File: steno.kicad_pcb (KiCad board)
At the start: 4 copper layers, 220 x 59 mm, 83 parts, among them J1 USB_C_Receptacle_USB2.0_14P, U1 W25Q16JVSS, U2 AP2127N-3.3, U3 RP2040, Y1 12 MHz

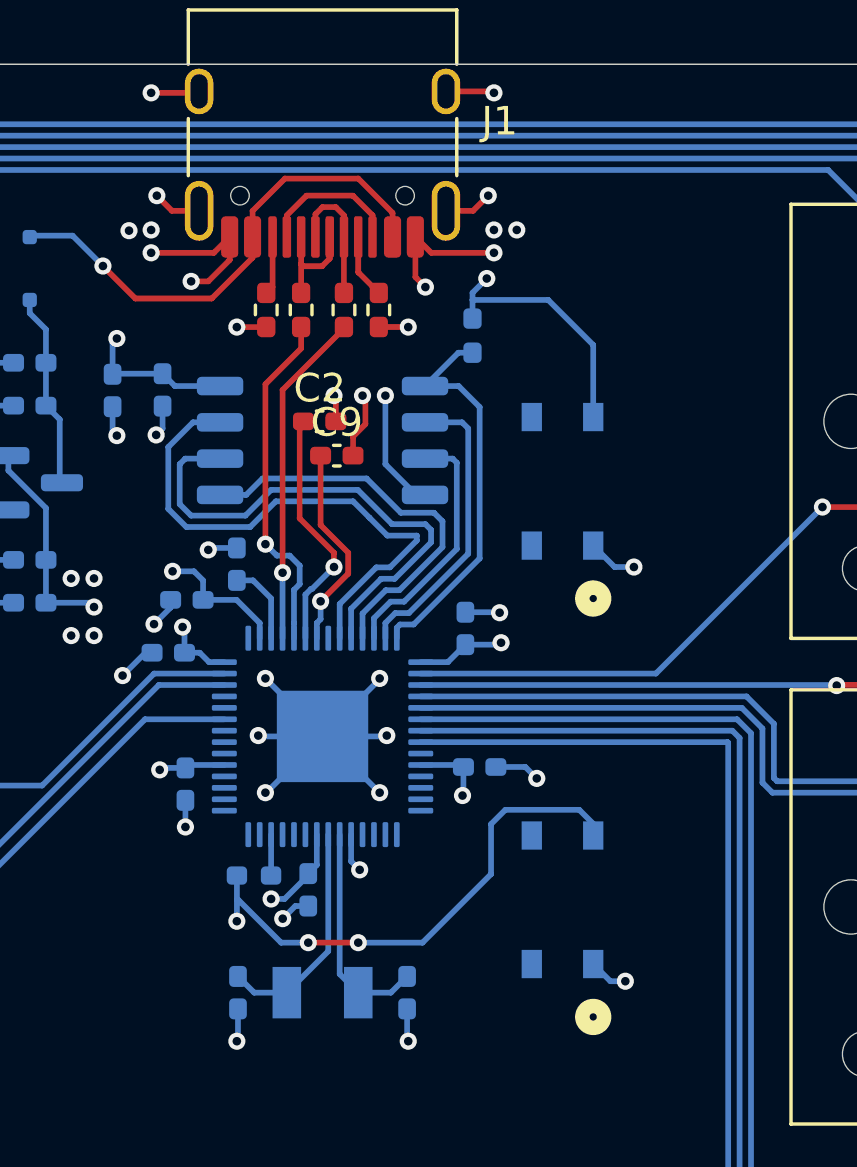
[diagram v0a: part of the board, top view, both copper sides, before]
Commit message: added status LED / Potential final changes
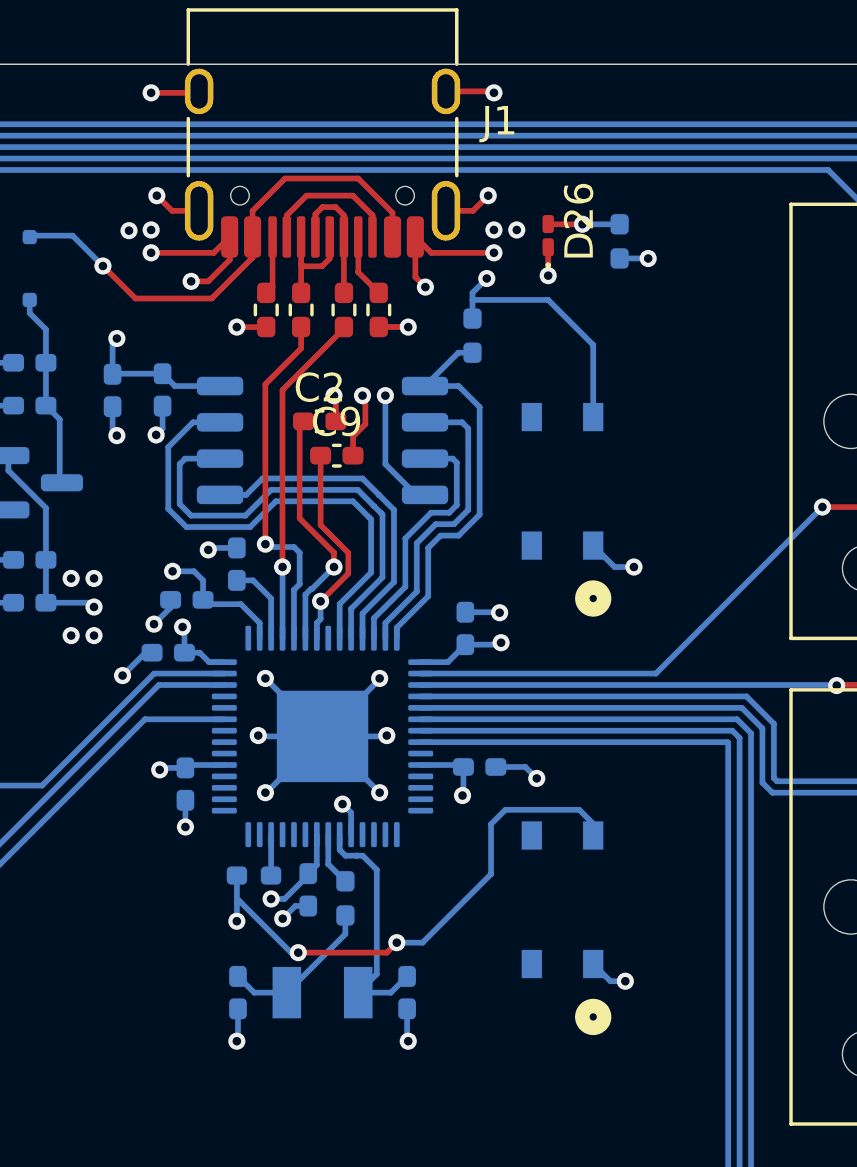
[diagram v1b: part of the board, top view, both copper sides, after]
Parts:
- added D26: LED, LED_SMD:LED_0201_0603Metric_Pad0.64x0.40mm_HandSolder, F.Cu at (158.0, 82.9)
- added R7: 1k Ohms, Resistor_SMD:R_0402_1005Metric_Pad0.72x0.64mm_HandSolder, B.Cu at (150.9, 106.1)
- added R8: 120 Ohm, Resistor_SMD:R_0402_1005Metric_Pad0.72x0.64mm_HandSolder, B.Cu at (160.5, 83.1)
- C10, C9: value 110nF -> 110n
- C11, C12, C2: value 110nF -> 100n
- R4, R5: value 27 Ohm -> 270 Ohm
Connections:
- C8 pad 1: Net-(U3-XOUT) -> Net-(C8-Pad1)
- Y1 pad 1: Net-(U3-XOUT) -> Net-(C8-Pad1)
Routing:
- net Net-(U3-XOUT): track 8.08 -> 1.88 mm
- net Net-(C8-Pad1): track 0.00 -> 5.50 mm
- net Net-(D26-A): track 0.00 -> 2.50 mm, vias 0 -> 1
- net QSPI_SDO: track 14.2 -> 11.7 mm
- net QSPI_SCLK: track 18.0 -> 15.7 mm
- net QSPI_SD3: track 19.2 -> 17.0 mm
- net +3.3V: track 74.2 -> 75.4 mm, vias 14 -> 15
- net Net-(U3-XIN): track 7.75 -> 8.64 mm
- net GND: track 66.2 -> 67.1 mm, vias 44 -> 45

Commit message: Made changes based on feedback and RP2040 doc.
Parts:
- removed the C1 at (139.8, 87.3)
- removed the C1 at (155.6, 101.5)
- removed the C1 at (149.6, 105.8)
- removed the C1 at (144.7, 97.5)
- removed the C1 at (145.3, 102.1)
- removed C10: 110n, Capacitor_SMD:C_0402_1005Metric_Pad0.74x0.62mm_HandSolder
- removed the C2 at (150.0, 89.4)
- removed the C2 at (142.8, 88.3)
- removed C4: 2.2uF, Capacitor_SMD:C_0402_1005Metric_Pad0.74x0.62mm_HandSolder
- removed C6: 47uF, Capacitor_SMD:C_0402_1005Metric_Pad0.74x0.62mm_HandSolder
- removed J1: USB_C_Receptacle_USB2.0_14P, Connector_USB:USB_C_Receptacle_HRO_TYPE-C-31-M-12
- removed U2: AP2127N-3.3, Package_TO_SOT_SMD:SOT-23
- added C1: 100n, Capacitor_SMD:C_0402_1005Metric, B.Cu at (149.6, 120.5)
- added C13: 100n, Capacitor_SMD:C_0402_1005Metric, B.Cu at (144.9, 111.5)
- added C14: 100n, Capacitor_SMD:C_0402_1005Metric, B.Cu at (155.3, 111.2)
- added C15: 100n, Capacitor_SMD:C_0402_1005Metric, B.Cu at (154.9, 115.5)
- added C16: 100n, Capacitor_SMD:C_0402_1005Metric, B.Cu at (148.6, 120.5)
- added C17: 100n, Capacitor_SMD:C_0402_1005Metric, B.Cu at (146.0, 107.9)
- added C18: 1u, Capacitor_SMD:C_0402_1005Metric, B.Cu at (145.4, 109.7)
- added C19: 1u, Capacitor_SMD:C_0402_1005Metric, B.Cu at (152.7, 106.6)
- added C2: 100n, Capacitor_SMD:C_0402_1005Metric, B.Cu at (153.6, 98.4)
- added J2: USB_C_Receptacle_USB2.0_16P, Connector_USB:USB_C_Receptacle_HCTL_HC-TYPE-C-16P-01A, F.Cu at (150.1, 78.9)
- added U4: NCP1117-3.3_SOT223, Package_TO_SOT_SMD:SOT-223-3_TabPin2, B.Cu at (141.8, 98.0)
- C11, C12: footprint Capacitor_SMD:C_0402_1005Metric_Pad0.74x0.62mm_HandSolder -> Capacitor_SMD:C_0402_1005Metric
- C3, C5: value 1uF -> 10u; footprint Capacitor_SMD:C_0402_1005Metric_Pad0.74x0.62mm_HandSolder -> Capacitor_SMD:C_0603_1608Metric
- C7, C8: value 15pF -> 10p; footprint Capacitor_SMD:C_0402_1005Metric_Pad0.74x0.62mm_HandSolder -> Capacitor_SMD:C_0402_1005Metric
- C9: value 110n -> 100n; footprint Capacitor_SMD:C_0402_1005Metric_Pad0.74x0.62mm_HandSolder -> Capacitor_SMD:C_0402_1005Metric; moved to B.Cu
- D1: footprint Diode_SMD:D_SOD-323F -> Diode_SMD:D_SOD-123F
- D10, D11, D12, D13, D14, D15, D16, D17, D18, D19, D2, D20, D21, D22, D23, D24, D25, D3, D4, D5, D6, D7, D8, D9: footprint Diode_SMD:D_SOD-123 -> Diode_SMD:D_SOD-123F
- LED1: renamed from D26; footprint LED_SMD:LED_0201_0603Metric_Pad0.64x0.40mm_HandSolder -> LED_SMD:LED_0402_1005Metric
- R1, R6, R7, R8: footprint Resistor_SMD:R_0402_1005Metric_Pad0.72x0.64mm_HandSolder -> Resistor_SMD:R_0402_1005Metric
- R2, R3: footprint Resistor_SMD:R_0402_1005Metric_Pad0.72x0.64mm_HandSolder -> Resistor_SMD:R_0402_1005Metric; moved to B.Cu
- R4, R5: value 270 Ohm -> 27 Ohm; footprint Resistor_SMD:R_0402_1005Metric_Pad0.72x0.64mm_HandSolder -> Resistor_SMD:R_0402_1005Metric; moved to B.Cu
- Y1: value 12 MHz -> Crystal_GND24; footprint Crystal:Crystal_SMD_3215-2Pin_3.2x1.5mm -> Crystal:Crystal_SMD_3225-4Pin_3.2x2.5mm_HandSoldering
- moved R4 22.7 mm to (147.0, 107.9)
- moved R5 22.4 mm to (148.0, 107.9)
- moved BOOTSEL1 21.6 mm to (159.7, 113.1)
- moved C12 21.2 mm to (145.2, 115.5), turned to -90 degrees
- moved RST1 19.2 mm to (140.5, 113.1), turned to -90 degrees
- moved C9 17.4 mm to (149.0, 107.9), turned to 90 degrees
- moved Y1 16.8 mm to (150.1, 126.2), turned to 0 degrees
- moved R7 14.4 mm to (150.6, 120.5)
- moved U1 14.0 mm to (157.7, 101.8)
- moved R6 13.8 mm to (146.9, 119.1)
- moved U3 13.6 mm to (150.1, 114.1)
- moved C7 13.6 mm to (151.9, 122.9), turned to 180 degrees
- moved C8 13.6 mm to (148.2, 122.9), turned to 0 degrees
- moved C11 12.5 mm to (151.3, 106.6), turned to 90 degrees
- moved R1 12.4 mm to (161.3, 97.3)
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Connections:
- C12 pad 1: Net-(U3-VREG_VOUT) -> +3.3V
- U3 pad 23: unconnected-(U3-DVDD-Pad23) -> +1.1V
- U3 pad 38: unconnected-(U3-GPIO26/ADC0-Pad38) -> ROW_2
- U3 pad 39: unconnected-(U3-GPIO27/ADC1-Pad39) -> ROW_1
- U3 pad 40: ROW_2 -> unconnected-(U3-GPIO28/ADC2-Pad40)
- U3 pad 41: ROW_1 -> unconnected-(U3-GPIO29/ADC3-Pad41)
- U3 pad 45: Net-(U3-VREG_VOUT) -> +1.1V
- U3 pad 50: unconnected-(U3-DVDD-Pad23)_1 -> +1.1V
- Y1 pad 2: Net-(U3-XIN) -> GND
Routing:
- net GND: track 67.1 -> 24.0 mm, vias 45 -> 30
- net +1.1V: track 0.00 -> 32.9 mm
- net Net-(J2-D--PadA7): track 4.73 -> 33.6 mm, vias 0 -> 1
- net Net-(J2-D+-PadA6): track 3.85 -> 31.4 mm, vias 0 -> 2
- net ROW_3: track 109.0 -> 126.0 mm
- net COL_1: track 350.1 -> 334.5 mm
- net COL_2: track 298.7 -> 283.7 mm
- net COL_3: track 241.4 -> 226.9 mm
- net ROW_4: track 114.7 -> 128.1 mm
- net ROW_1: track 99.2 -> 110.2 mm
- net D+: track 12.5 -> 2.67 mm, vias 1 -> 0
- net QSPI_SD2: track 8.89 -> 18.4 mm
- net QSPI_SS: track 14.0 -> 23.4 mm
- net QSPI_SD1: track 10.5 -> 19.9 mm
- net D-: track 11.8 -> 3.40 mm, vias 1 -> 0
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- added copper zone on B.Cu, net GND
- added copper zone on F.Cu, net GND
- removed copper zone on B.Cu, net (none)
- removed copper zone on F.Cu, net (none)
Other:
- board text added: "To reason out ahead of time what you want to do is just as harmful as stickingr a pin a ripening piece of fruit - that it's only a usless waste of energy and r juice"
- board text added: "stenΩ 0.1"

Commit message: Gerber plot(s) and drill files.
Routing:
- net +3.3V: vias 26 -> 34
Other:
- board text added: "stenΩ 0.2"
- board text removed: "stenΩ 0.1"
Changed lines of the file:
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@@
 			(outputformat 1)
 			(mirror no)
-			(drillshape 1)
+			(drillshape 0)
 			(scaleselection 1)
-			(outputdirectory "")
+			(outputdirectory "./")
 		)
 	)
@@
 		(tags "capacitor")
 		(property "Reference" "C14"
-			(at 0 1.16 0)
+			(at 0.4 1.3 0)
 			(layer "B.SilkS")
 			(effects
@@
 		(tags "capacitor")
 		(property "Reference" "C12"
-			(at 0.3 -1.3 90)
+			(at 1.65 0.7 180)
 			(layer "B.SilkS")
 			(effects
@@
 		(tags "capacitor")
 		(property "Reference" "C1"
-			(at -1.59 -0.04 180)
+			(at -1.6 0.4 180)
 			(layer "B.SilkS")
 			(effects
@@
 		(tags "capacitor")
 		(property "Reference" "C18"
-			(at 0 1.16 0)
+			(at 2.4 0 0)
 			(layer "B.SilkS")
 			(effects
@@
 		(tags "resistor")
 		(property "Reference" "R3"
-			(at 0 1.17 90)
+			(at 2.025 -0.075 90)
 			(layer "B.SilkS")
 			(effects
@@
 		(tags "resistor")
 		(property "Reference" "R2"
-			(at 0 1.17 90)
+			(at 2.025 -0.055 90)
 			(layer "B.SilkS")
 			(effects
@@
 		(tags "resistor")
 		(property "Reference" "R1"
-			(at 0.1 -1.2 90)
+			(at 0.075 1.2 90)
 			(layer "B.SilkS")
 			(effects
@@
 		(tags "capacitor")
 		(property "Reference" "C13"
-			(at 2.38 -0.1 0)
+			(at 0.48 -1.2 0)
 			(layer "B.SilkS")
 			(effects
@@
 		(tags "capacitor")
 		(property "Reference" "C16"
-			(at 0.02 1.91 0)
+			(at 0 1.9 0)
 			(layer "B.SilkS")
 			(effects
@@
 		(tags "capacitor")
 		(property "Reference" "C15"
-			(at 0 1.16 90)
+			(at 1.75 -0.925 180)
 			(layer "B.SilkS")
 			(effects
@@
 		(tags "D_SOD-123F")
 		(property "Reference" "D1"
-			(at -0.127 1.905 270)
+			(at 0 -2.06 270)
 			(layer "B.SilkS")
 			(effects
@@
 		(tags "resistor")
 		(property "Reference" "R7"
-			(at 0 1.17 90)
+			(at 1.6 0.5 180)
 			(layer "B.SilkS")
 			(effects
@@
 		(layer "User.4")
 	)
-	(gr_text "stenΩ 0.1\n"
+	(gr_text "stenΩ 0.2\n"
 		(at 139.1 100.6 0)
 		(layer "F.SilkS")
@@
 			(justify left bottom)
 		)
-		(render_cache "stenΩ 0.1\n" 0
+		(render_cache "stenΩ 0.2\n" 0
 			(polygon
 				(pts
@@
 			(polygon
 				(pts
-					(xy 159.577015 99.24) (xy 159.577015 97.729113) (xy 160.34931 97.729113) (xy 160.34931 92.770983)
-					(xy 159.568588 94.270635) (xy 159.568588 92.412923) (xy 160.286296 91.069588) (xy 160.978907 91.069588)
-					(xy 160.978907 97.729113) (xy 161.591652 97.729113) (xy 161.591652 99.24)
+					(xy 159.514 99.24) (xy 159.514 97.740348) (xy 160.676657 94.6624) (xy 160.77509 94.325526) (xy 160.833115 93.953023)
+					(xy 160.852878 93.532044) (xy 160.840874 93.236543) (xy 160.806507 92.986127) (xy 160.750113 92.770983)
+					(xy 160.675155 92.604295) (xy 160.586322 92.503753) (xy 160.47937 92.468611) (xy 160.369898 92.504866)
+					(xy 160.278244 92.608972) (xy 160.2002 92.782219) (xy 160.141754 93.005762) (xy 160.105853 93.270506)
+					(xy 160.093222 93.587732) (xy 159.463625 93.587732) (xy 159.479059 93.075537) (xy 159.523555 92.62206)
+					(xy 159.595882 92.217041) (xy 159.694981 91.854032) (xy 159.815939 91.547607) (xy 159.960964 91.293803)
+					(xy 160.120708 91.110383) (xy 160.299319 90.997069) (xy 160.500436 90.957725) (xy 160.696248 90.994072)
+					(xy 160.868433 91.098178) (xy 161.020673 91.265471) (xy 161.159297 91.500083) (xy 161.274694 91.786192)
+					(xy 161.369085 92.127648) (xy 161.438176 92.509507) (xy 161.480491 92.933539) (xy 161.495115 93.408946)
+					(xy 161.48354 93.835806) (xy 161.448794 94.254233) (xy 161.390151 94.668262) (xy 161.309813 95.056078)
+					(xy 161.198055 95.455954) (xy 161.050165 95.870914) (xy 160.319818 97.729113) (xy 161.528637 97.729113)
+					(xy 161.528637 99.24)
 				)
 			)
@@
 	)
 	(via
+		(at 156.4 120)
+		(size 0.6)
+		(drill 0.3)
+		(layers "F.Cu" "B.Cu")
+		(free yes)
+		(net "+3.3V")
+	)
+	(via
 		(at 161.1 95.1)
 		(size 0.6)
@@
 	)
 	(via
+		(at 164.4 91.6)
+		(size 0.6)
+		(drill 0.3)
+		(layers "F.Cu" "B.Cu")
+		(free yes)
+		(net "+3.3V")
+	)
+	(via
+		(at 154.8 120)
+		(size 0.6)
+		(drill 0.3)
+		(layers "F.Cu" "B.Cu")
+		(free yes)
+		(net "+3.3V")
+	)
+	(via
 		(at 142.575 104.925)
 		(size 0.6)
@@
 	)
 	(via
+		(at 164.4 93.2)
+		(size 0.6)
+		(drill 0.3)
+		(layers "F.Cu" "B.Cu")
+		(free yes)
+		(net "+3.3V")
+	)
+	(via
+		(at 164.4 92.4)
+		(size 0.6)
+		(drill 0.3)
+		(layers "F.Cu" "B.Cu")
+		(free yes)
+		(net "+3.3V")
+	)
+	(via
 		(at 140.3 126.1)
 		(size 0.6)
@@
 	)
 	(via
+		(at 154 120)
+		(size 0.6)
+		(drill 0.3)
+		(layers "F.Cu" "B.Cu")
+		(free yes)
+		(net "+3.3V")
+	)
+	(via
 		(at 142.55 97.175)
 		(size 0.6)
@@
 	)
 	(via
+		(at 164.4 90.8)
+		(size 0.6)
+		(drill 0.3)
+		(layers "F.Cu" "B.Cu")
+		(free yes)
+		(net "+3.3V")
+	)
+	(via
 		(at 149.836438 119.14662)
 		(size 0.6)
@@
 		(net "+3.3V")
 	)
+	(via
+		(at 155.6 120)
+		(size 0.6)
+		(drill 0.3)
+		(layers "F.Cu" "B.Cu")
+		(free yes)
+		(net "+3.3V")
+	)

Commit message: Savepoint!
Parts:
- removed U4: NCP1117-3.3_SOT223, Package_TO_SOT_SMD:SOT-223-3_TabPin2
- added U2: AMS1117-3.3, Package_TO_SOT_SMD:SOT-223-3_TabPin2, B.Cu at (141.8, 98.0)
- C18, C19: footprint Capacitor_SMD:C_0402_1005Metric -> Capacitor_SMD:C_0603_1608Metric
- D1: footprint Diode_SMD:D_SOD-123F -> Diode_SMD:D_SMA
- D10, D11, D12, D13, D14, D15, D16, D17, D18, D19, D2, D20, D21, D22, D23, D24, D25, D3, D4, D5, D6, D7, D8, D9: footprint Diode_SMD:D_SOD-123F -> Diode_SMD:D_SOD-123
- Y1: footprint Crystal:Crystal_SMD_3225-4Pin_3.2x2.5mm_HandSoldering -> Crystal:Crystal_SMD_3225-4Pin_3.2x2.5mm
- moved R1 13.9 mm to (155.9, 110.1), turned to 180 degrees
- moved D1 2.56 mm to (141.8, 88.0), turned to 180 degrees
- moved R6 0.85 mm to (147.6, 119.6), turned to -90 degrees
- moved C18 0.81 mm to (144.6, 109.8)
- moved C19 0.76 mm to (153.0, 105.9), turned to 0 degrees
- moved C14 0.60 mm to (155.9, 111.2)
- moved C11 0.40 mm to (150.9, 106.6)
- moved C13 0.40 mm to (144.9, 111.9)
- turned BOOTSEL1 to -90 degrees
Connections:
- BOOTSEL1 pad 1: GND -> QSPI_SS
- BOOTSEL1 pad 2: +3.3V -> (no net)
- BOOTSEL1 pad 3: (no net) -> GND
- BOOTSEL1 pad 4: (no net) -> GND
- R6 pad 1: +3.3V -> Net-(U3-RUN)
- R6 pad 2: Net-(U3-RUN) -> +3.3V
- REF** pad 1: (no net) -> GND (x4)
- RST1 pad 1: GND -> (no net)
- RST1 pad 2: +3.3V -> Net-(U3-RUN)
- RST1 pad 3: (no net) -> GND
- RST1 pad 4: (no net) -> GND
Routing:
- net +3.3V: track 69.4 -> 39.5 mm
- net Net-(U3-RUN): track 2.25 -> 12.6 mm
- net Net-(D1-A): track 14.1 -> 19.4 mm
- net GND: track 24.0 -> 19.1 mm, vias 30 -> 27
- net QSPI_SS: track 23.4 -> 27.2 mm
- net ROW_4: track 128.1 -> 125.3 mm
- net ROW_3: track 126.0 -> 123.2 mm
- net ROW_1: track 110.2 -> 107.5 mm
- net ROW_2: track 94.6 -> 92.0 mm
- net ROW_5: track 124.6 -> 122.4 mm
- net Net-(U3-XIN): track 11.4 -> 13.4 mm
- net QSPI_SD3: track 14.1 -> 15.3 mm
- net QSPI_SD2: track 18.4 -> 17.2 mm
- net QSPI_SD1: track 19.9 -> 18.7 mm
- net QSPI_SCLK: track 12.7 -> 13.8 mm
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
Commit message: Init Commit!
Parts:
- removed BOOTSEL1, RST1: SW_Push, 3rd_party_footprints:SW4_PTS815 SJM 250 SMTR LFS_CNK
- removed C1, C11, C12, C13, C14, C15, C16, C17, C2, C9: 100n, Capacitor_SMD:C_0402_1005Metric
- removed C18, C19: 1u, Capacitor_SMD:C_0603_1608Metric
- removed C3, C5: 10u, Capacitor_SMD:C_0603_1608Metric
- removed C7, C8: 10p, Capacitor_SMD:C_0402_1005Metric
- removed D1: D, Diode_SMD:D_SMA
- removed J2: USB_C_Receptacle_USB2.0_16P, Connector_USB:USB_C_Receptacle_HCTL_HC-TYPE-C-16P-01A
- removed LED1: LED, LED_SMD:LED_0402_1005Metric
- removed R1, R6, R7: 1k Ohms, Resistor_SMD:R_0402_1005Metric
- removed R2, R3: 5.1K Ohm, Resistor_SMD:R_0402_1005Metric
- removed R4, R5: 27 Ohm, Resistor_SMD:R_0402_1005Metric
- removed R8: 120 Ohm, Resistor_SMD:R_0402_1005Metric
- removed U1: W25Q16JVSS, Package_SO:SOIC-8_5.3x5.3mm_P1.27mm
- removed U3: RP2040, Package_DFN_QFN:QFN-56-1EP_7x7mm_P0.4mm_EP3.2x3.2mm
- removed Y1: Crystal_GND24, Crystal:Crystal_SMD_3225-4Pin_3.2x2.5mm
- added SW1: Switch, Button_Switch_SMD:SW_SPST_PTS810, B.Cu at (162.8, 87.9)
- U2: value AMS1117-3.3 -> RP2040_Pro_Micro; footprint Package_TO_SOT_SMD:SOT-223-3_TabPin2 -> 3rd_party_footprints:RP2040_Pro_Micro; moved to F.Cu
- moved U2 9.39 mm to (150.0, 93.4), turned to 0 degrees
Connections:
- U2 pad 1: GND -> unconnected-(U2-gp0-Pad1)
- U2 pad 2: +3.3V -> unconnected-(U2-gp1-Pad2)
- U2 pad 3: Net-(D1-K) -> GND
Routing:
- net +3.3V: track 39.5 -> 0.00 mm, vias 34 -> 0
- net +1.1V: track 33.7 -> 0.00 mm
- net Net-(J2-D--PadA7): track 33.6 -> 0.00 mm, vias 1 -> 0
- net Net-(J2-D+-PadA6): track 31.4 -> 0.00 mm, vias 2 -> 0
- net QSPI_SS: track 27.2 -> 0.00 mm
- net ROW_3: track 123.2 -> 101.6 mm, vias 10 -> 9
- net Net-(D1-A): track 19.4 -> 0.00 mm, vias 3 -> 0
- net QSPI_SD1: track 18.7 -> 0.00 mm
- net QSPI_SD2: track 17.2 -> 0.00 mm
- net QSPI_SD3: track 15.3 -> 0.00 mm
- net ROW_4: track 125.3 -> 110.1 mm, vias 8 -> 7
- net ROW_1: track 107.5 -> 93.5 mm, vias 8 -> 9
- net QSPI_SCLK: track 13.8 -> 0.00 mm
- net Net-(U3-XIN): track 13.4 -> 0.00 mm
- net COL_5: track 127.1 -> 113.8 mm, vias 0 -> 1
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- removed copper zone on In2.Cu, net +3.3V
- removed copper zone on In1.Cu, net GND
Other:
- copper layers 4 -> 2
- board text removed: "To reason out ahead of time what you want to do is just as harmful as stickingr a pin a ripening piece of fruit - that it's only a usless waste of energy and r juice"
